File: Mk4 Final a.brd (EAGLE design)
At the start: 121.6 x 82.5 mm, 318 parts, among them IC1 MSP432E401, IC10 TPD3E001DRL, IC11 TLV9002IDGK, IC12 SN74HC4066D, IC13 TPA2006D1, IC14 MX25R1635FM1IL0, IC15 CC3120R, IC16 TMP102AIDRLR, IC17 OPT3001DNPR, IC18 DRV5055A1QDBZR, IC2 AS4C4M16SA-7TCN, IC3 HDC2080DMBR, IC4 TCA9555RGER, IC5 SIM800C24 S2-10686-Z1L09, IC6 MX25R8035FM1IH1, IC7 TPD3E001DRL, IC8 BQ25601, IC9 TPS62822DLCR, J1 78723-1001, J10 H4P-SMD-2.0, J11 M02X2, J2 ER-CON50HT-1, J3 2x5 1.27mm, J4 GSM-COIL-ANT, J5 S2B-PH-SM4-TB(LF)(SN), J7 SMA-142-0711-821/826, J8 H4P-SMD-2.0, J9 PJ-393-A, Q1 2N7002PW, Q2 2N7002PW, Q3 CSD25402Q3A, Q8 CSD13202Q2, SW1 JOYSTICK, U1 ZX62-B-5PA(33), U4 MIC-6MM, U5 LDMS1540S-01-R8-0.8-R, X1 ABS07-32.768KHZ-T, X2 ABM8G-25.000MHZ-B4Y-T, X3 ABS07-32.768KHZ-T, X4 ABM8-40.000MHZ-10-1-U-T

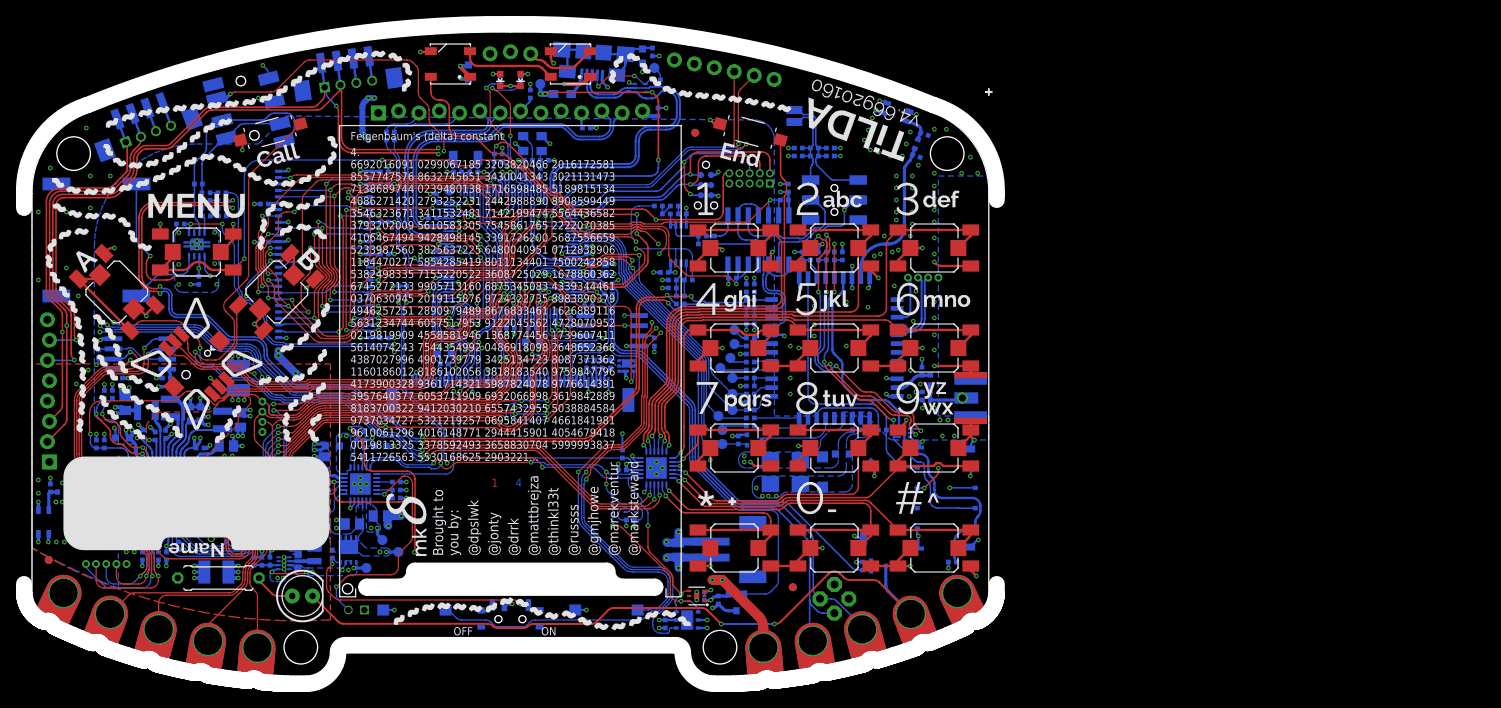
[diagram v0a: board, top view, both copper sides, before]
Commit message: Few DNP's and schematic for print
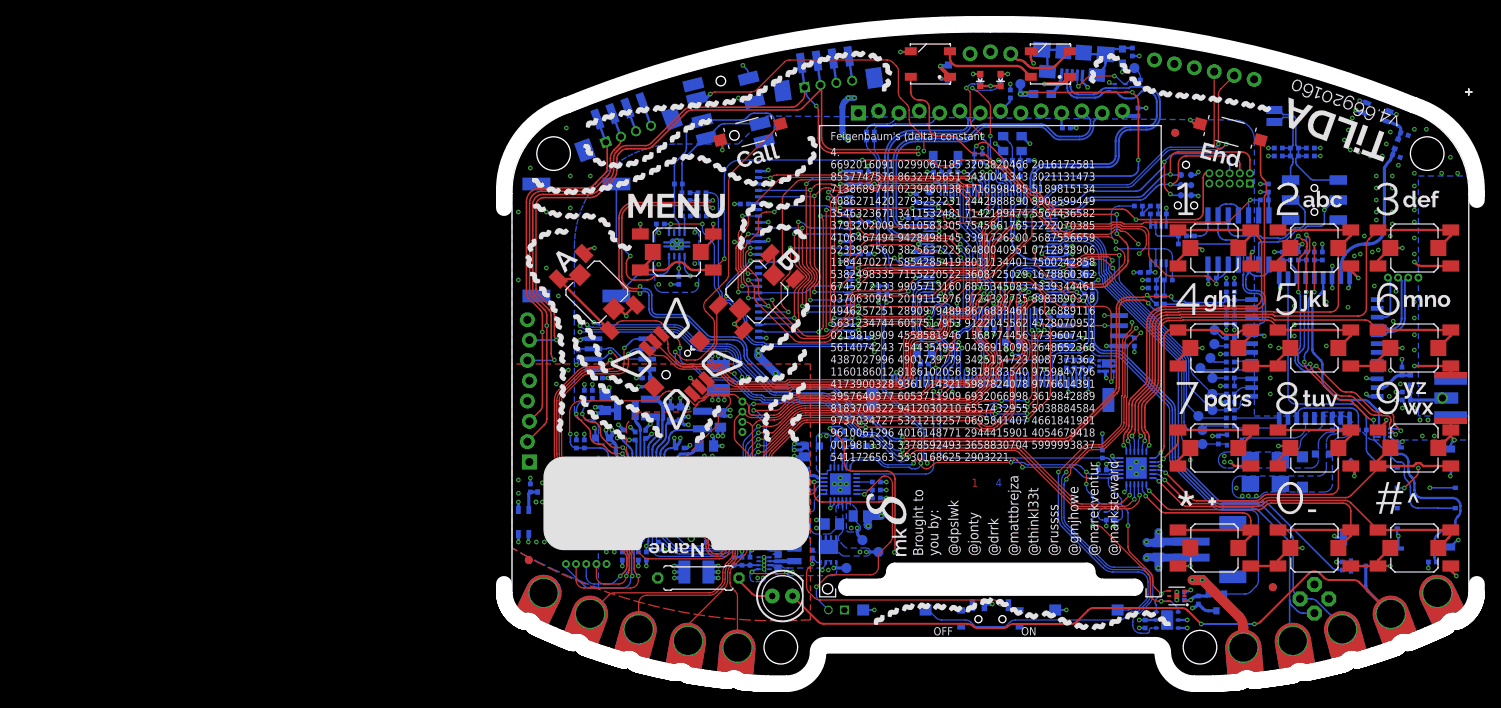
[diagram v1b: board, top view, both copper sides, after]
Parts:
- moved J3 60.0 mm to (89.9, 62.2)
- moved LOGO3 60.0 mm to (76.4, 57.4)
- moved U1 60.0 mm to (70.4, 78.0)
- moved ANT1 60.0 mm to (1.65, 19.2)
- moved ANT2 60.0 mm to (108.2, 70.5)
- moved ARTWORK1 60.0 mm to (20.8, 39.0)
- moved ARTWORK2 60.0 mm to (60.0, 0.00)
- moved ARTWORK3 60.0 mm to (48.1, 37.0)
- moved ARTWORK4 60.0 mm to (37.5, 35.0)
- moved ARTWORK5 60.0 mm to (37.5, 28.0)
- moved ARTWORK6 60.0 mm to (60.0, 0.00)
- moved ARTWORK7 60.0 mm to (104.2, 66.8)
- moved BATT 60.0 mm to (59.5, 12.0)
- moved C1 60.0 mm to (54.8, 75.5)
- moved C10 60.0 mm to (50.8, 52.6)
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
